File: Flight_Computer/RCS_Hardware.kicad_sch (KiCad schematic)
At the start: 55 parts, among them J1 SWD, J2 TYPE-C-31-M-12, J3 I2C, J4 5V, J5 GND, J8 Conn_01x05_Male, U1 STM32F401CCU6, U2 AMS1117-3.3, U4 BNO055, U5 W25Q32JVSS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

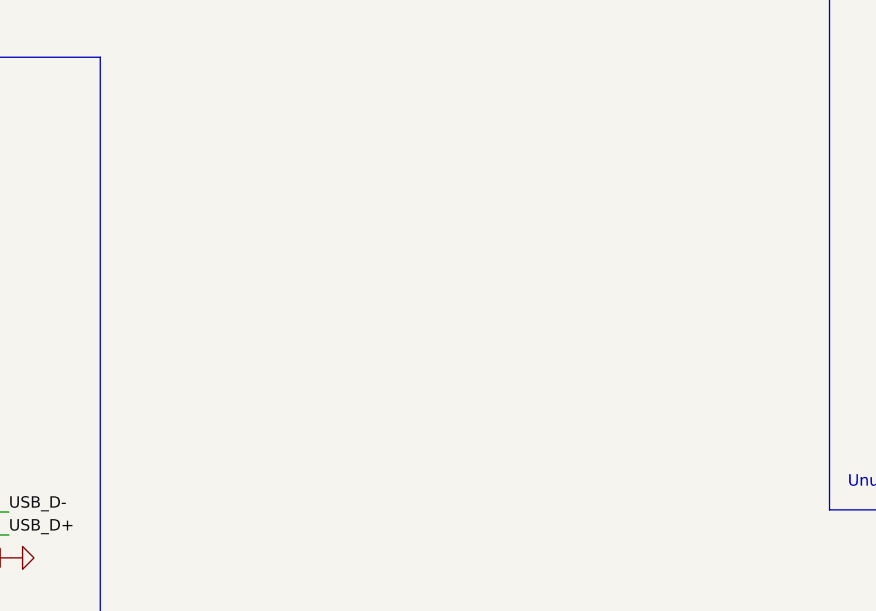
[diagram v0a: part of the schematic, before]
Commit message: Added rotary encoder symbol and schematic
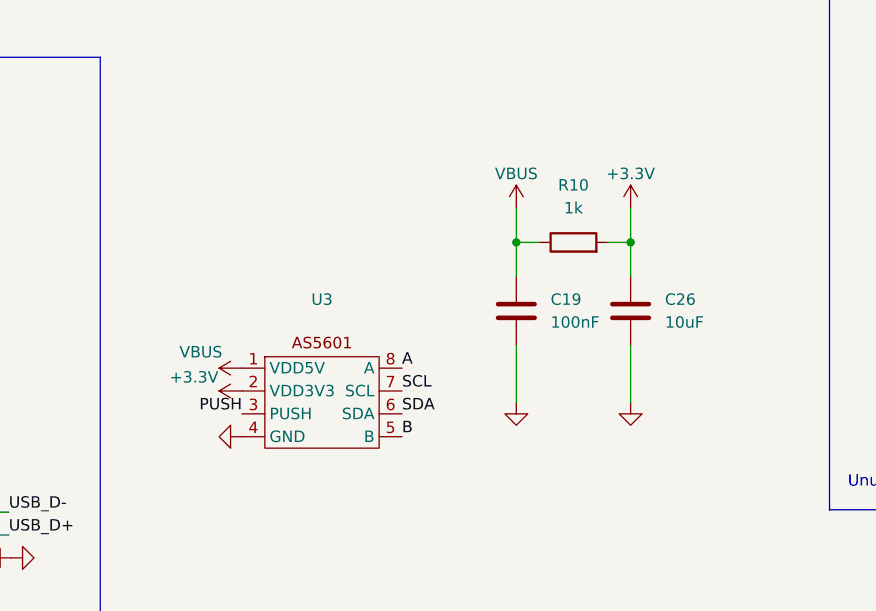
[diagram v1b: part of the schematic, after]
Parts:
- added C19: 100nF, Capacitor_SMD:C_0805_2012Metric, symbol Device:C
- added C26: 10uF, Capacitor_SMD:C_0805_2012Metric, symbol Device:C
- added R10: 1k, Resistor_SMD:R_0402_1005Metric, symbol Device:R
- added U3: ~, symbol Library:AS5601
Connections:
- net +3.3V: now also C26.1, R10.2, U3.2 (VDD3V3)
- net GND: now also C19.2, C26.2, U3.4 (GND)
- net SCL: now also U3.7 (SCL)
- net SDA: now also U3.6 (SDA)
- net VBUS: now also C19.1, R10.1, U3.1 (VDD5V)
- new net A: U3.8 (A)
- new net B: U3.5 (B)
- new net PUSH: U3.3 (PUSH)

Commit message: changes
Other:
- note added: "Add 3v3 circuit from ARES"
- note added: "Add ribbon connector"
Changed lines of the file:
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@@
+		)
+	)
+	(text "Add 3v3 circuit from ARES"
+		(exclude_from_sim no)
+		(at 341.376 127.508 0)
+		(effects
+			(font
+				(size 1.27 1.27)
+			)
 		)
 	)
@@
 		)
 	)
+	(text "Add ribbon connector"
+		(exclude_from_sim no)
+		(at 338.836 123.19 0)
+		(effects
+			(font
+				(size 1.27 1.27)
+			)
+		)
+	)

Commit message: Added Uart and LM2576
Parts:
- removed C21, C24: 0.1uF, Capacitor_SMD:C_0402_1005Metric, symbol Device:C
- removed C22: 2.2nF, Capacitor_SMD:C_0402_1005Metric, symbol Device:C
- removed C25: 10nF, Capacitor_SMD:C_0402_1005Metric, symbol Device:C
- removed U6: MPU-6050, Sensor_Motion:InvenSense_QFN-24_4x4mm_P0.5mm, symbol Sensor_Motion:MPU-6050
- added C27: 100uF, Capacitor_SMD:C_0805_2012Metric, symbol Device:C
- added C28: 1000uF, Capacitor_SMD:CP_Elec_10x10.5, symbol Device:C
- added D4: SS34, Diode_SMD:D_SMA, symbol Diode:SS34
- added J6: FC_M/P, Connector_FFC-FPC:Molex_200528-0080_1x08-1MP_P1.00mm_Horizontal, symbol Connector_Generic:Conn_01x08
- added J7: FC_RF, Connector_FFC-FPC:Molex_200528-0080_1x08-1MP_P1.00mm_Horizontal, symbol Connector_Generic:Conn_01x08
- added L1: 100uH, Inductor_SMD:L_TaiTech_TMPC1265_13.5x12.5mm, symbol Device:L
- added U8: LM2576S-3.3, Package_TO_SOT_SMD:TO-263-5_TabPin3, symbol Regulator_Switching:LM2576S-3.3
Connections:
- net +3.3V: now also C28.2, J6.2 (Pin_2), J7.2 (Pin_2), L1.2, U8.4 (FB)
- net GND: now also C27.1, C28.1, D4.2 (A), J6.8 (Pin_8), J7.8 (Pin_8), U8.3 (GND), U8.5 (~{ON}/OFF)
- net VBUS: now also J6.1 (Pin_1), J7.1 (Pin_1)
- new net: D4.1 (K), L1.1, U8.2 (OUT)
- new net +BATT: C27.2, U8.1 (VIN)
- new net MOTOR_NRST: J6.7 (Pin_7)
- new net MOTOR_SCL: J6.6 (Pin_6)
- new net MOTOR_SDA: J6.5 (Pin_5)
- new net RADIO_NRST: J7.7 (Pin_7)
- new net RX_RADIO: J7.5 (Pin_5)
- new net S1_MP: J6.3 (Pin_3)
- new net S1_RF: J7.3 (Pin_3)
- new net S2_MP: J6.4 (Pin_4)
- new net S2_RF: J7.4 (Pin_4)
- new net TX_RADIO: J7.6 (Pin_6)
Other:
- note added: "AS5601 Breakout"
- note added: "Battery Regulator"
- note added: "UART CONNECTORS"
- note removed: "Add 3v3 circuit from ARES"
- note removed: "Add ribbon connector"
- note removed: "Unused"

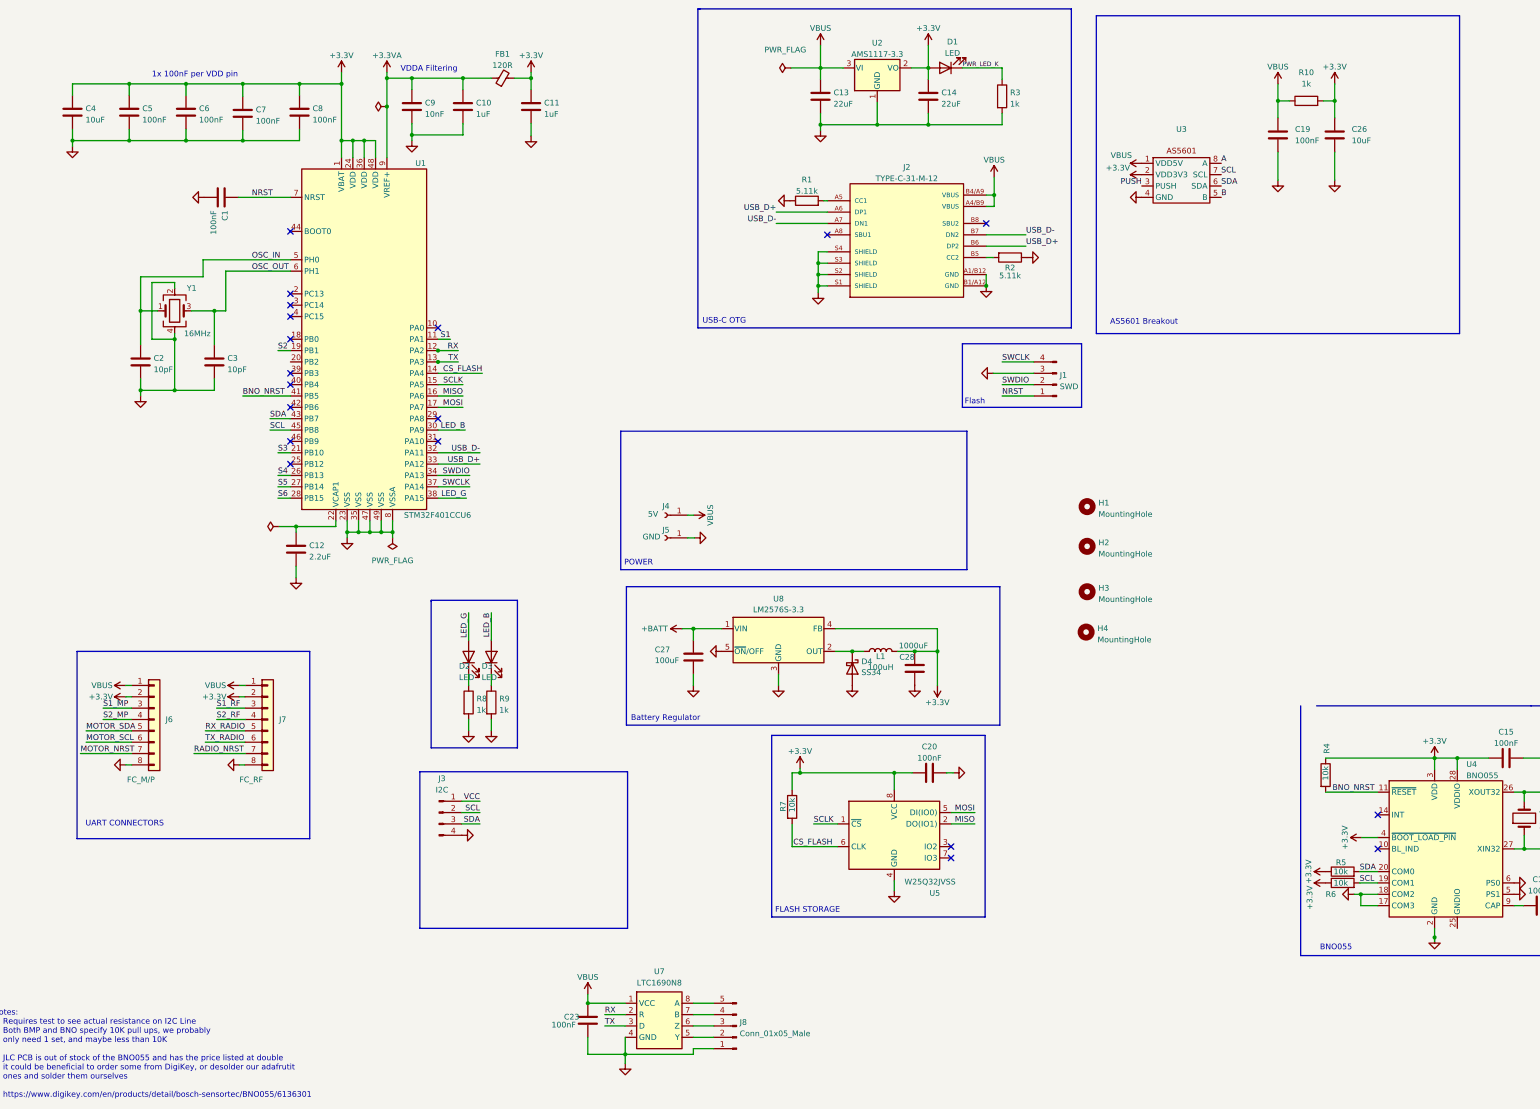
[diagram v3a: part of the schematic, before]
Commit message: Added AS5601 and motor conn
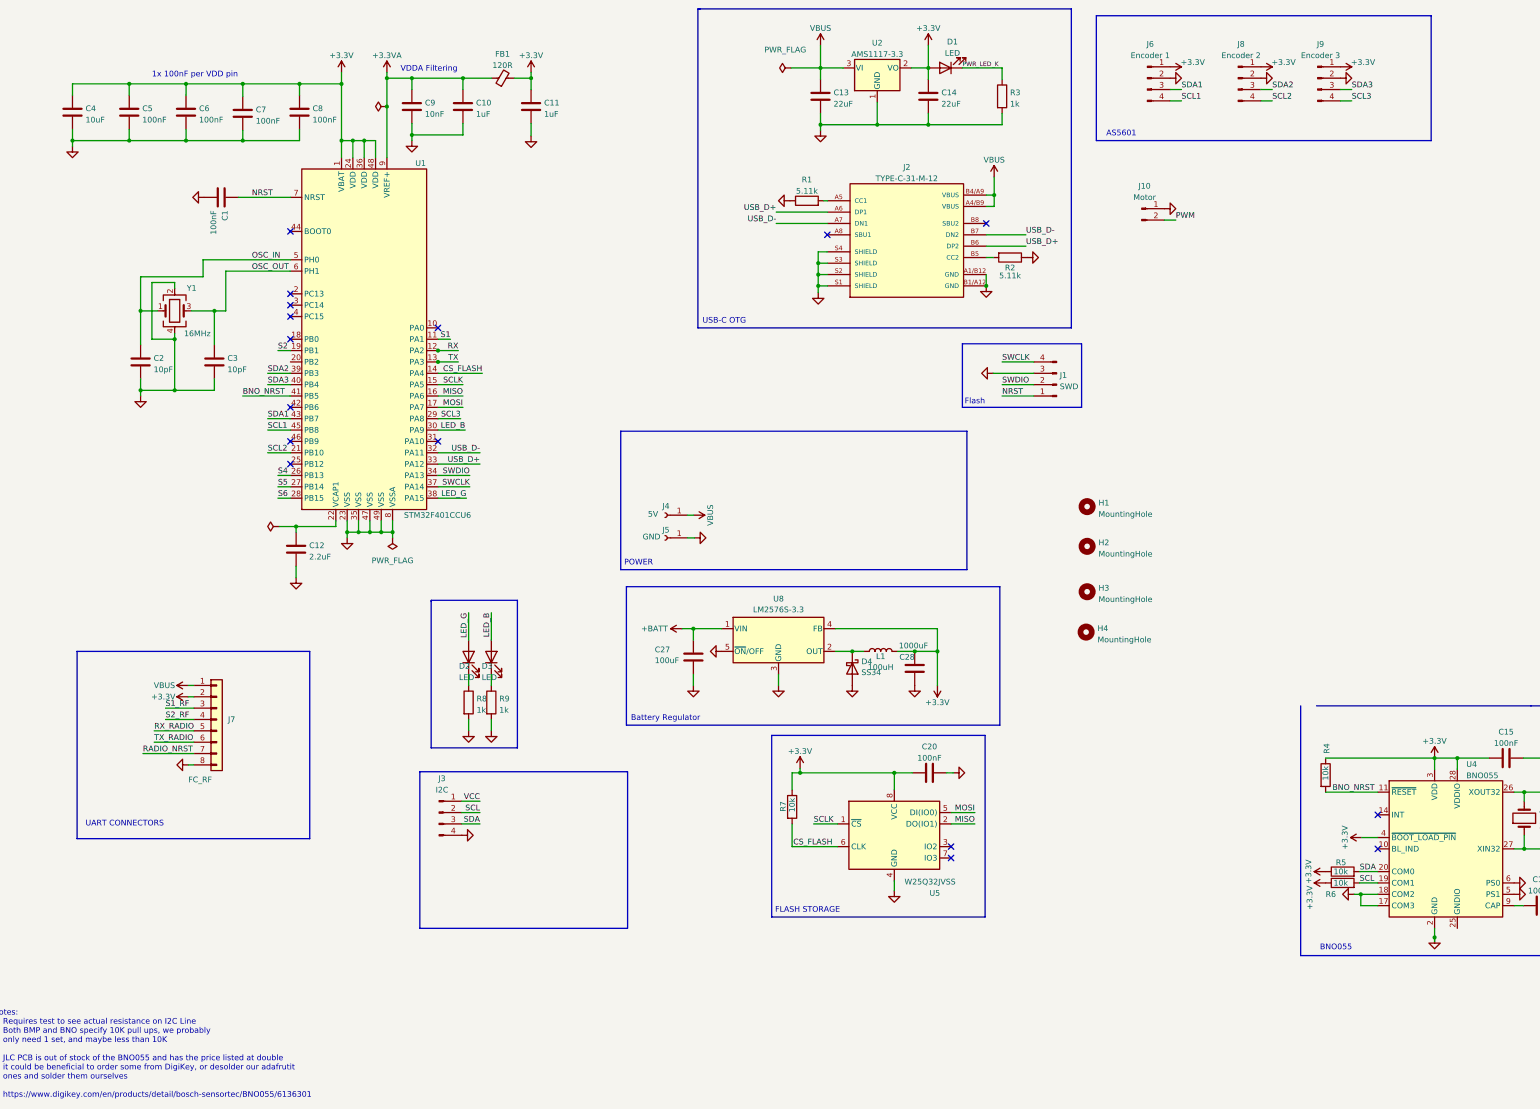
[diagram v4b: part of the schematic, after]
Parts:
- removed C19: 100nF, Capacitor_SMD:C_0805_2012Metric, symbol Device:C
- removed C23: 100nF, Capacitor_SMD:C_0402_1005Metric, symbol Device:C
- removed C26: 10uF, Capacitor_SMD:C_0805_2012Metric, symbol Device:C
- removed J6: FC_M/P, Connector_FFC-FPC:Molex_200528-0080_1x08-1MP_P1.00mm_Horizontal, symbol Connector_Generic:Conn_01x08
- removed J8: Conn_01x05_Male, Connector_PinHeader_2.54mm:PinHeader_1x05_P2.54mm_Vertical, symbol Connector:Conn_01x05_Male
- removed R10: 1k, Resistor_SMD:R_0402_1005Metric, symbol Device:R
- removed U3: ~, symbol Library:AS5601
- removed U7: LTC1690N8, LTC1690N8:LTC1690N8, symbol lt1690n8:LT1690N8
- added J10: Motor, symbol Connector:Conn_01x02_Pin
- added J6: Encoder 1, symbol Connector:Conn_01x04_Pin
- added J8: Encoder 2, symbol Connector:Conn_01x04_Pin
- added J9: Encoder 3, symbol Connector:Conn_01x04_Pin
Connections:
- net +3.3V: now also J6.1 (Pin_1), J8.1 (Pin_1), J9.1 (Pin_1)
- net GND: now also J10.1 (Pin_1), J6.2 (Pin_2), J8.2 (Pin_2), J9.2 (Pin_2)
- net SCL: no longer U1.45 (PB8)
- net SDA: no longer U1.43 (PB7)
- net SCL3: now reaches U1.29 (PA8)
- net SCL3: now also J9.4 (Pin_4)
- net SDA2: now reaches U1.39 (PB3)
- net SDA2: now also J8.3 (Pin_3)
- net SDA3: now reaches U1.40 (PB4)
- net SDA3: now also J9.3 (Pin_3)
- net S3 renamed SCL2
- net SCL2: now also J8.4 (Pin_4)
- new net PWM: J10.2 (Pin_2)
- new net SCL1: J6.4 (Pin_4), U1.45 (PB8)
- new net SDA1: J6.3 (Pin_3), U1.43 (PB7)
- no-connect marks 19 -> 16
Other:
- note added: "AS5601"
- note removed: "AS5601 Breakout"
- moved on the sheet: J7

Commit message: Motor connector
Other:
- note added: "Motor"
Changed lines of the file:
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@@
+	)
+	(rectangle
+		(start 266.7 57.15)
+		(end 294.64 74.93)
+		(stroke
+			(width 0)
+			(type default)
+		)
+		(fill
+			(type none)
+		)
 	)
 	(rectangle
@@
 		(effects
 			(font
+				(size 1.27 1.27)
+			)
+		)
+	)
+	(text "Motor\n"
+		(exclude_from_sim no)
+		(at 270.256 72.898 0)
+		(effects
+			(font

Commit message: Added new to do
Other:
- note added: "A/B to GPIO"
- note added: "Add new encoder pins"
- note added: "Change Battery Regulator to 5V"
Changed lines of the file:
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@@
+		)
+	)
+	(text "Add new encoder pins"
+		(exclude_from_sim no)
+		(at 324.612 61.468 0)
+		(effects
+			(font
+				(size 1.27 1.27)
+			)
 		)
 	)
@@
 		)
 	)
+	(text "Change Battery Regulator to 5V\n"
+		(exclude_from_sim no)
+		(at 329.438 67.056 0)
+		(effects
+			(font
+				(size 1.27 1.27)
+			)
+		)
+	)
 	(text "Battery Regulator"
 		(exclude_from_sim no)
@@
 		)
 	)
+	(text "A/B to GPIO\n"
+		(exclude_from_sim no)
+		(at 320.294 64.262 0)
+		(effects
+			(font
+				(size 1.27 1.27)
+			)
+		)
+	)

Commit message: New
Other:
- note added: "24 V In"
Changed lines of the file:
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@@
+		)
+	)
+	(text "24 V In\n"
+		(exclude_from_sim no)
+		(at 318.008 69.342 0)
+		(effects
+			(font
+				(size 1.27 1.27)
+			)
 		)
 	)

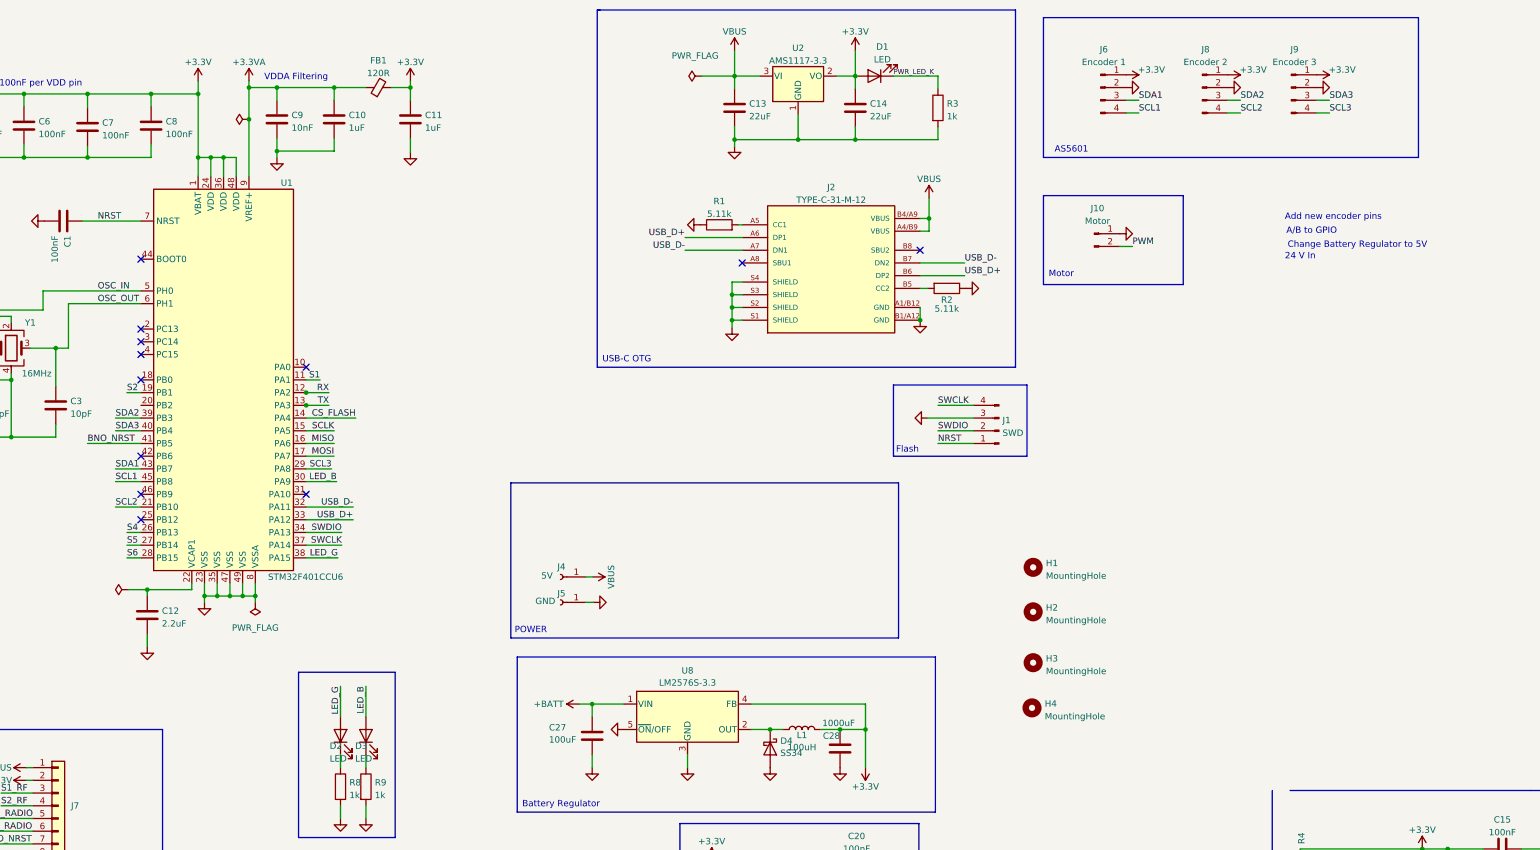
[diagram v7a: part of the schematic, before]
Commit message: New battery circuit, updated encoders
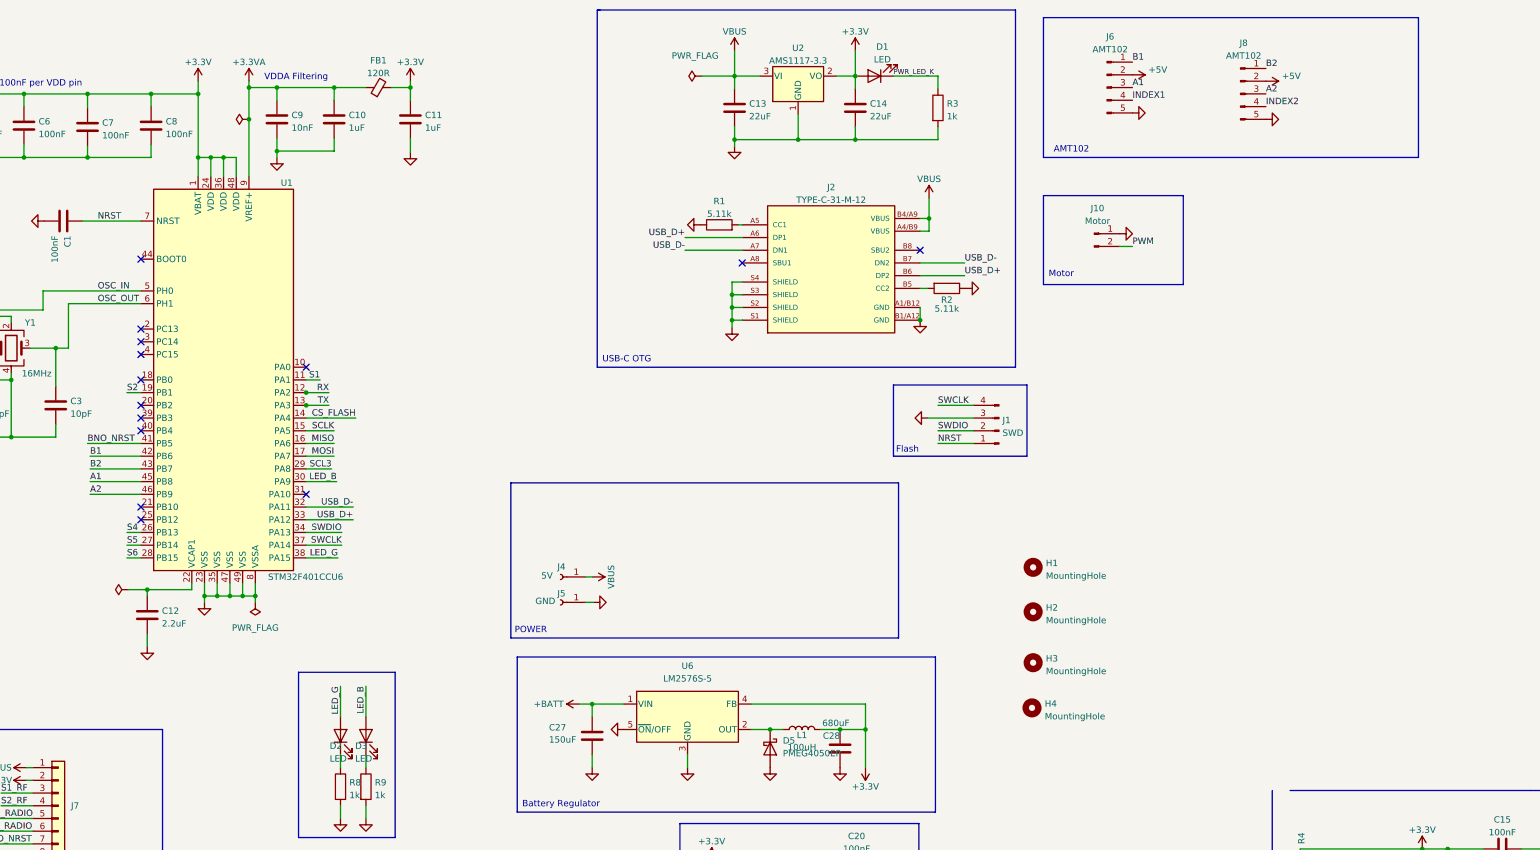
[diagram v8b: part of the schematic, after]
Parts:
- removed D4: SS34, Diode_SMD:D_SMA, symbol Diode:SS34
- removed J6: Encoder 1, symbol Connector:Conn_01x04_Pin
- removed J8: Encoder 2, symbol Connector:Conn_01x04_Pin
- removed J9: Encoder 3, symbol Connector:Conn_01x04_Pin
- removed U8: LM2576S-3.3, Package_TO_SOT_SMD:TO-263-5_TabPin3, symbol Regulator_Switching:LM2576S-3.3
- added D5: PMEG4050EP, Diode_SMD:D_SOD-128, symbol Diode:PMEG4050EP
- added J6, J8: AMT102, symbol Connector:Conn_01x05_Pin
- added U6: LM2576S-5, Package_TO_SOT_SMD:TO-263-5_TabPin3, symbol Regulator_Switching:LM2576S-5
- C27: value 100uF -> 150uF
- C28: value 1000uF -> 680uF
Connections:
- net +3.3V: now also U6.4 (FB)
- net +BATT: now also U6.1 (VIN)
- net GND: now also D5.2 (A), J6.5 (Pin_5), J8.5 (Pin_5), U6.3 (GND), U6.5 (~{ON}/OFF)
- net at L1.1: now also D5.1 (K), U6.2 (OUT)
- net B1: now reaches U1.42 (PB6)
- net B1: now also J6.1 (Pin_1)
- net A2: now reaches U1.46 (PB9)
- net A2: now also J8.3 (Pin_3)
- net SCL1 renamed A1
- net A1: now also J6.3 (Pin_3)
- net SCL2: no longer names the net of U1.21 (PB10)
- net SDA1 renamed B2
- net B2: now also J8.1 (Pin_1)
- net SDA2: no longer names the net of U1.39 (PB3)
- net SDA3: no longer names the net of U1.40 (PB4)
- new net +5V: J6.2 (Pin_2), J8.2 (Pin_2)
- new net INDEX1: J6.4 (Pin_4)
- new net INDEX2: J8.4 (Pin_4)
- no-connect marks 16 -> 18
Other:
- note added: "AMT102"
- note removed: "24 V In"
- note removed: "A/B to GPIO"
- note removed: "AS5601"
- note removed: "Add new encoder pins"
- note removed: "Change Battery Regulator to 5V"
